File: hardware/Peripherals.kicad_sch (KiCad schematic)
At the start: 29 parts

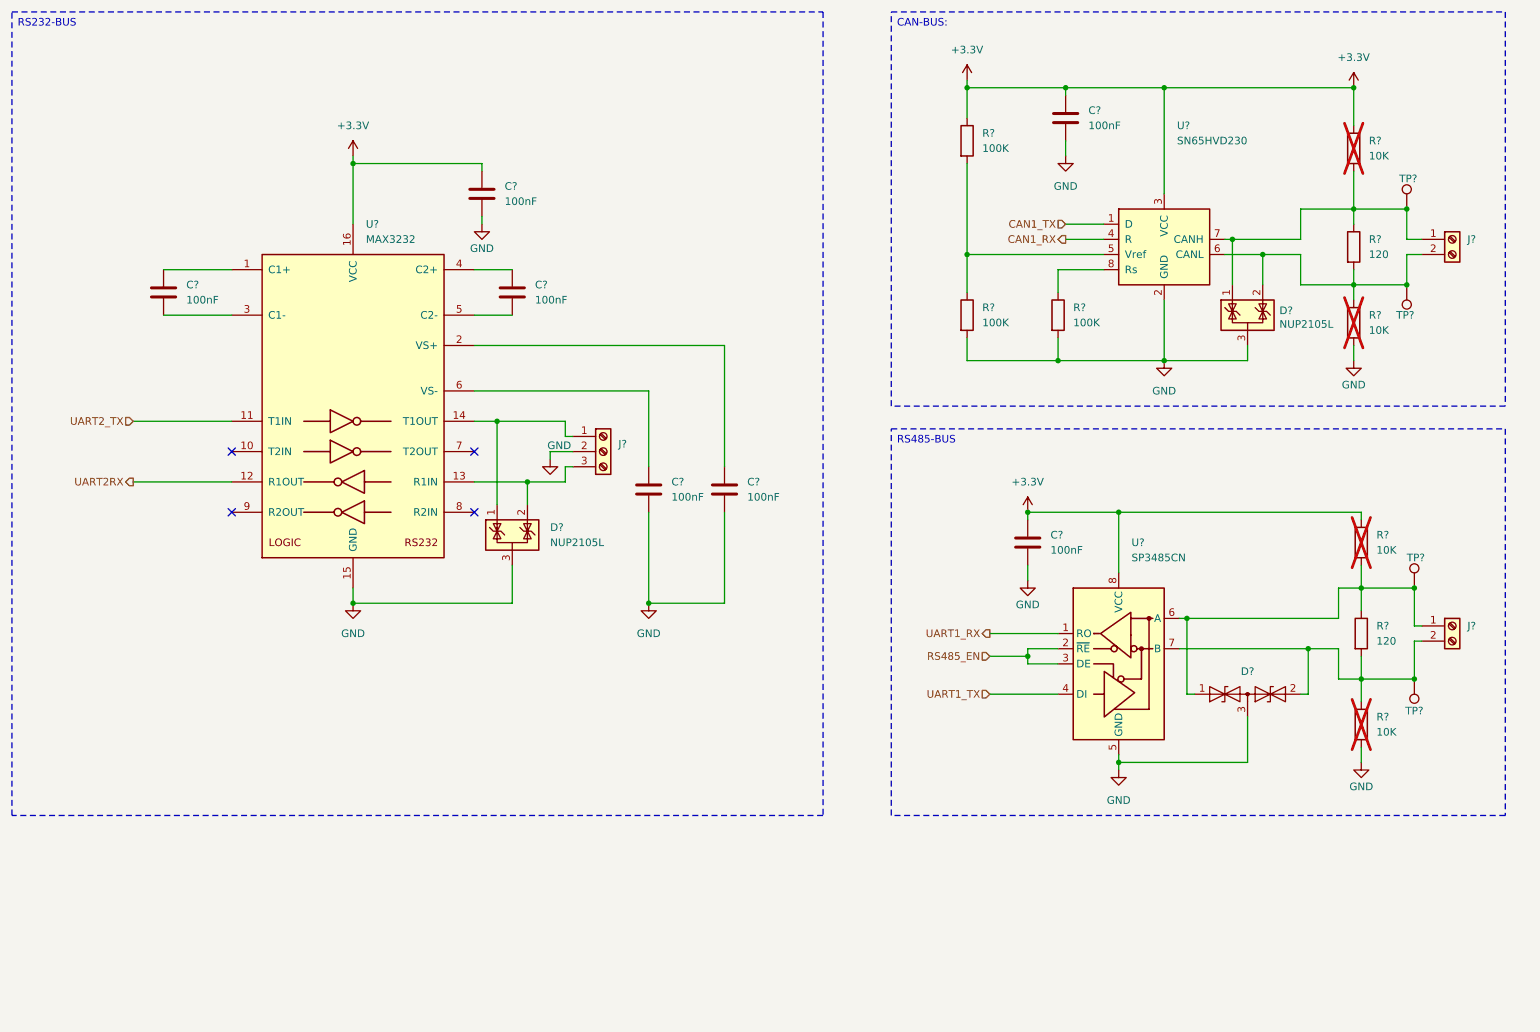
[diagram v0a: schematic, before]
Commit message: Change ESP32 module to stand-alone, change regulator for wide input range, modify location of certain things on MCU_Unit.
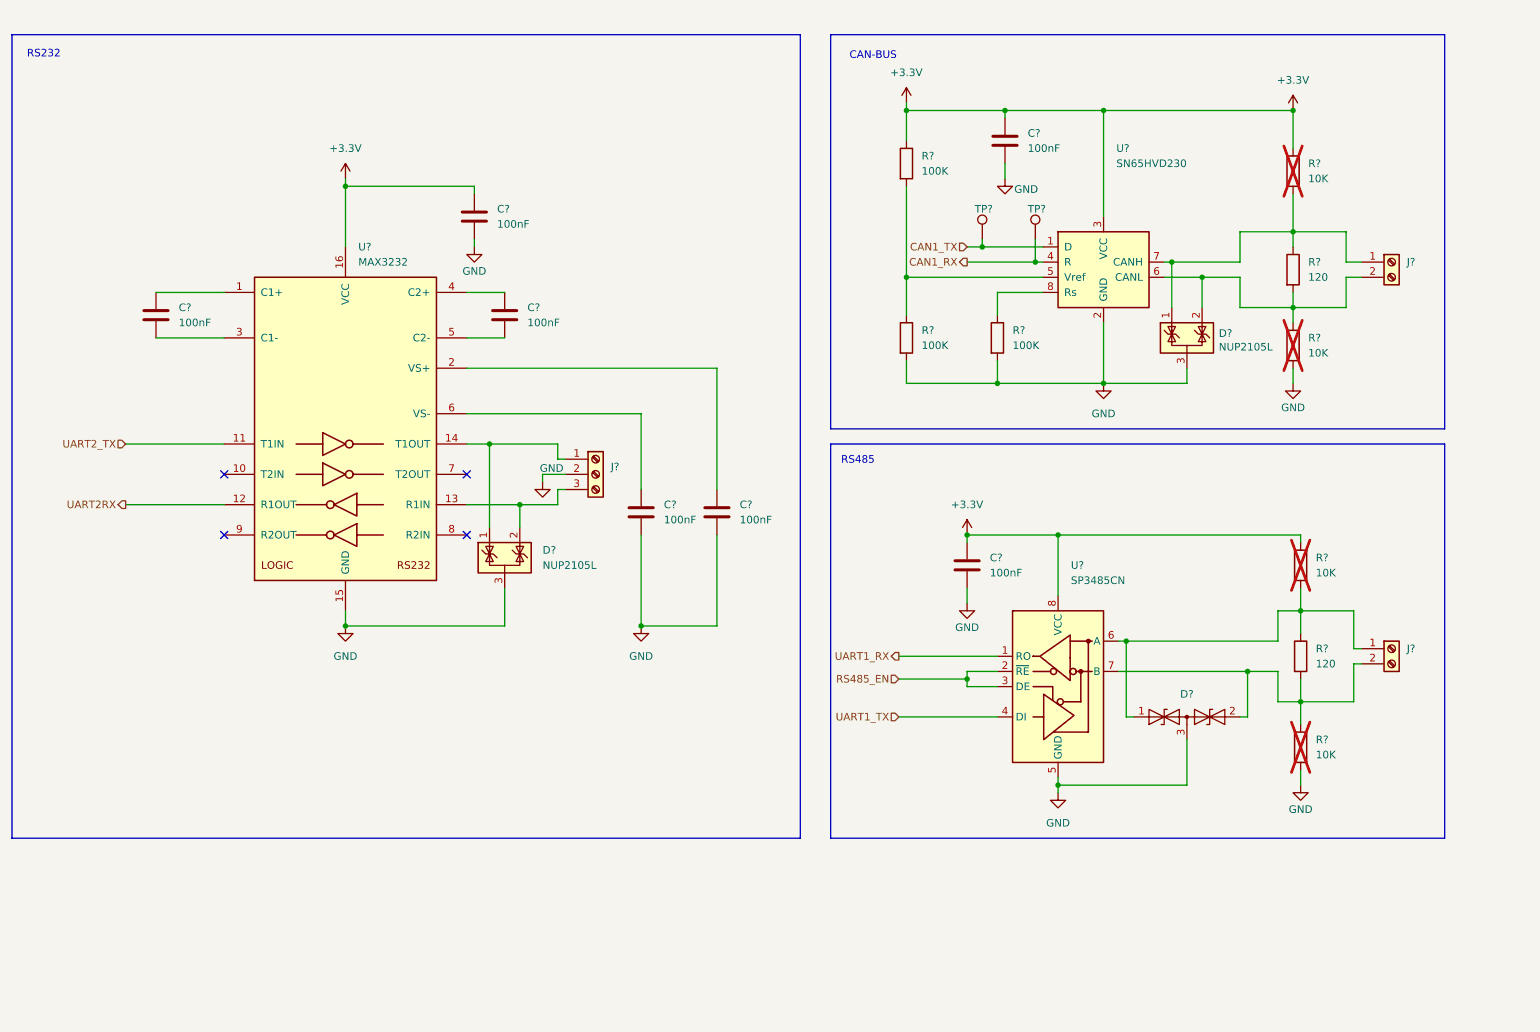
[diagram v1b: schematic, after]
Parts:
- removed TP? (x3): TestPoint, symbol Connector:TestPoint
- added TP?: TestPoint, symbol Connector:TestPoint
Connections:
- net CAN1_RX: now also TP?.1
- net CAN1_TX: now also TP?.1
- net at D?.2 (K), J?.2 (Pin_2), R?.1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: no longer TP?.1
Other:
- note added: "CAN-BUS"
- note added: "RS232"
- note added: "RS485"
- moved on the sheet: C?, D?, J?, R?, TP?, U?

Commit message: Assign footprints to some components and improvements.
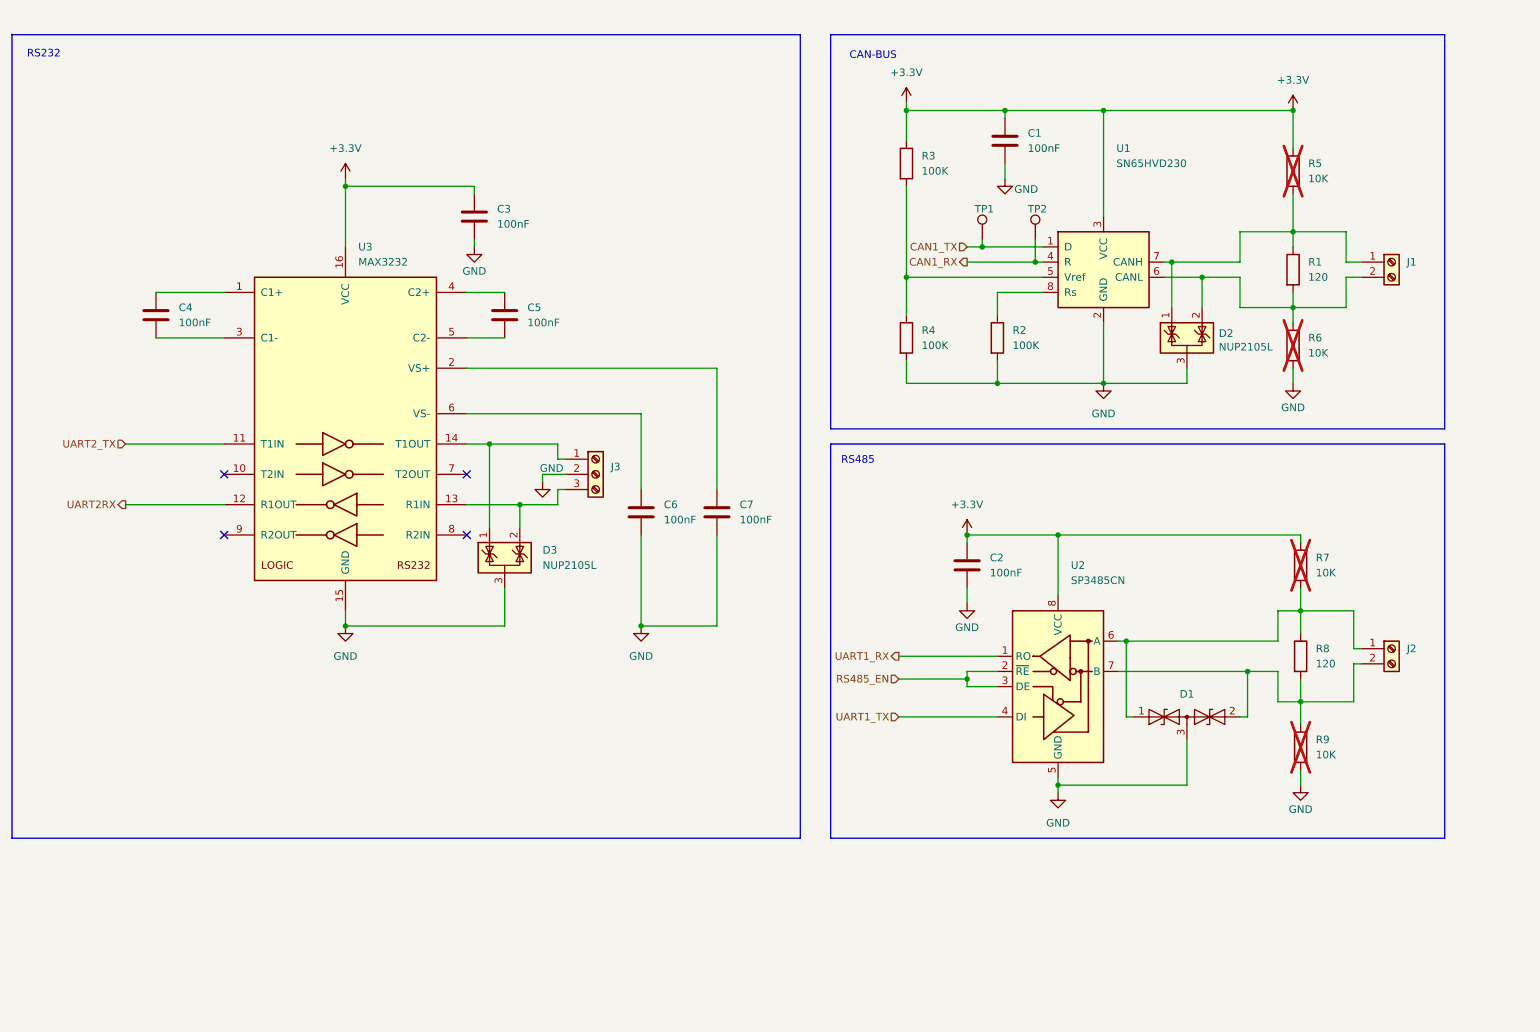
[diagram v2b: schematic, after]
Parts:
- R1, R2, R3, R4, R5, R6, R8: renamed from R?; footprint (none) -> Resistor_SMD:R_0805_2012Metric_Pad1.20x1.40mm_HandSolder
- U3: renamed from U?; footprint (none) -> Package_SO:TSSOP-16_4.4x5mm_P0.65mm
- gave numbers to parts that had none: 19
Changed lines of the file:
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@@
 		(dnp no)
 		(fields_autoplaced yes)
-		(property "Reference" "#PWR?"
+		(property "Reference" "#PWR013"
 			(at 130.81 130.81 0)
 			(effects
@@
 		(dnp no)
 		(fields_autoplaced yes)
-		(property "Reference" "#PWR?"
+		(property "Reference" "#PWR012"
 			(at 81.28 53.34 0)
 			(effects
@@
 		(dnp no)
 		(fields_autoplaced yes)
-		(property "Reference" "U?"
+		(property "Reference" "U3"
 			(at 83.4233 60.96 0)
 			(effects
@@
 			)
 		)
-		(property "Footprint" ""
+		(property "Footprint" "Package_SO:TSSOP-16_4.4x5mm_P0.65mm"
 			(at 82.55 118.11 0)
 			(effects
@@
 		(on_board yes)
 		(dnp no)
-		(property "Reference" "D?"
+		(property "Reference" "D2"
 			(at 227.584 75.438 0)
 			(effects
@@
 		(dnp no)
 		(fields_autoplaced yes)
-		(property "Reference" "C?"
+		(property "Reference" "C5"
 			(at 111.76 71.1199 0)
 			(effects
@@
 		(dnp no)
 		(fields_autoplaced yes)
-		(property "Reference" "#PWR?"
+		(property "Reference" "#PWR07"
 			(at 185.42 113.03 0)
 			(effects
@@
 		(on_board yes)
 		(dnp no)
-		(property "Reference" "U?"
+		(property "Reference" "U1"
 			(at 210.4233 44.45 0)
 			(effects
@@
 		(dnp no)
 		(fields_autoplaced yes)
-		(property "Reference" "R?"
+		(property "Reference" "R3"
 			(at 177.8 45.7199 0)
 			(effects
@@
 			)
 		)
-		(property "Footprint" ""
+		(property "Footprint" "Resistor_SMD:R_0805_2012Metric_Pad1.20x1.40mm_HandSolder"
 			(at 173.482 46.99 90)
 			(effects
@@
 		(dnp no)
 		(fields_autoplaced yes)
-		(property "Reference" "R?"
+		(property "Reference" "R2"
 			(at 193.04 74.9299 0)
 			(effects
@@
 			)
 		)
-		(property "Footprint" ""
+		(property "Footprint" "Resistor_SMD:R_0805_2012Metric_Pad1.20x1.40mm_HandSolder"
 			(at 188.722 76.2 90)
 			(effects
@@
 		(dnp yes)
 		(fields_autoplaced yes)
-		(property "Reference" "R?"
+		(property "Reference" "R5"
 			(at 242.57 46.9899 0)
 			(effects
@@
 			)
 		)
-		(property "Footprint" ""
+		(property "Footprint" "Resistor_SMD:R_0805_2012Metric_Pad1.20x1.40mm_HandSolder"
 			(at 238.252 48.26 90)
 			(effects
@@
 		(dnp no)
 		(fields_autoplaced yes)
-		(property "Reference" "J?"
+		(property "Reference" "J3"
 			(at 125.73 97.7899 0)
 			(effects
@@
 		(dnp no)
 		(fields_autoplaced yes)
-		(property "Reference" "#PWR?"
+		(property "Reference" "#PWR03"
 			(at 208.28 90.17 0)
 			(effects
@@
 		(dnp no)
 		(fields_autoplaced yes)
-		(property "Reference" "D?"
+		(property "Reference" "D1"
 			(at 222.25 135.89 0)
 			(effects
@@
 		(dnp yes)
 		(fields_autoplaced yes)
-		(property "Reference" "R?"
+		(property "Reference" "R9"
 			(at 243.84 143.5099 0)
 			(effects
@@
 		(dnp no)
 		(fields_autoplaced yes)
-		(property "Reference" "C?"
+		(property "Reference" "C7"
 			(at 147.32 104.1399 0)
 			(effects
@@
 		(on_board yes)
 		(dnp no)
-		(property "Reference" "#PWR?"
+		(property "Reference" "#PWR05"
 			(at 240.03 90.17 0)
 			(effects
@@
 		(dnp no)
 		(fields_autoplaced yes)
-		(property "Reference" "#PWR?"
+		(property "Reference" "#PWR01"
 			(at 175.26 40.64 0)
 			(effects
@@
 		(on_board yes)
 		(dnp no)
-		(property "Reference" "R?"
+		(property "Reference" "R8"
 			(at 243.84 128.2699 0)
 			(effects
@@
 			)
 		)
-		(property "Footprint" ""
+		(property "Footprint" "Resistor_SMD:R_0805_2012Metric_Pad1.20x1.40mm_HandSolder"
 			(at 239.522 129.54 90)
 			(effects
@@
 		(dnp no)
 		(fields_autoplaced yes)
-		(property "Reference" "C?"
+		(property "Reference" "C1"
 			(at 195.58 41.9099 0)
 			(effects
@@
 		(on_board yes)
 		(dnp no)
-		(property "Reference" "#PWR?"
+		(property "Reference" "#PWR09"
 			(at 191.77 55.88 0)
 			(effects
@@
 		(dnp no)
 		(fields_autoplaced yes)
-		(property "Reference" "C?"
+		(property "Reference" "C6"
 			(at 134.62 104.1399 0)
 			(effects
@@
 		(dnp no)
 		(fields_autoplaced yes)
-		(property "Reference" "C?"
+		(property "Reference" "C2"
 			(at 189.23 113.0299 0)
 			(effects
@@
 		(dnp no)
 		(fields_autoplaced yes)
-		(property "Reference" "C?"
+		(property "Reference" "C4"
 			(at 53.34 71.1199 0)
 			(effects
@@
 		(on_board yes)
 		(dnp no)
-		(property "Reference" "#PWR?"
+		(property "Reference" "#PWR08"
 			(at 185.42 127 0)
 			(effects
@@
 		(on_board yes)
 		(dnp no)
-		(property "Reference" "R?"
+		(property "Reference" "R1"
 			(at 242.57 63.4999 0)
 			(effects
@@
 			)
 		)
-		(property "Footprint" ""
+		(property "Footprint" "Resistor_SMD:R_0805_2012Metric_Pad1.20x1.40mm_HandSolder"
 			(at 238.252 64.77 90)
 			(effects
@@
 		(on_board yes)
 		(dnp no)
-		(property "Reference" "TP?"
+		(property "Reference" "TP1"
 			(at 186.69 54.61 0)
 			(effects
@@
 		(on_board yes)
 		(dnp no)
-		(property "Reference" "#PWR?"
+		(property "Reference" "#PWR06"
 			(at 241.3 157.48 0)
 			(effects
@@
 		(on_board yes)
 		(dnp no)
-		(property "Reference" "TP?"
+		(property "Reference" "TP2"
 			(at 195.58 54.61 0)
 			(effects
@@
 		(dnp no)
 		(fields_autoplaced yes)
-		(property "Reference" "R?"
+		(property "Reference" "R4"
 			(at 177.8 74.9299 0)
 			(effects
@@
 			)
 		)
-		(property "Footprint" ""
+		(property "Footprint" "Resistor_SMD:R_0805_2012Metric_Pad1.20x1.40mm_HandSolder"
 			(at 173.482 76.2 90)
 			(effects
@@
 		(dnp no)
 		(fields_autoplaced yes)
-		(property "Reference" "#PWR?"
+		(property "Reference" "#PWR04"
 			(at 200.66 158.75 0)
 			(effects
@@
 		(dnp no)
 		(fields_autoplaced yes)
-		(property "Reference" "J?"
+		(property "Reference" "J2"
 			(at 259.08 128.2699 0)
 			(effects
@@
 		(dnp yes)
 		(fields_autoplaced yes)
-		(property "Reference" "R?"
+		(property "Reference" "R7"
 			(at 243.84 113.0299 0)
 			(effects
@@
 		(dnp no)
 		(fields_autoplaced yes)
-		(property "Reference" "J?"
+		(property "Reference" "J1"
 			(at 259.08 63.4999 0)
 			(effects
@@
 		(on_board yes)
 		(dnp no)
-		(property "Reference" "#PWR?"
+		(property "Reference" "#PWR014"
 			(at 114.3 106.68 0)
 			(effects
@@
 		(on_board yes)
 		(dnp no)
-		(property "Reference" "#PWR?"
+		(property "Reference" "#PWR011"
 			(at 102.87 67.31 0)
 			(effects
@@
 		(dnp no)
 		(fields_autoplaced yes)
-		(property "Reference" "#PWR?"
+		(property "Reference" "#PWR02"
 			(at 240.03 41.91 0)
 			(effects
@@
 		(dnp no)
 		(fields_autoplaced yes)
-		(property "Reference" "C?"
+		(property "Reference" "C3"
 			(at 106.68 54.6099 0)
 			(effects
@@
 		(dnp no)
 		(fields_autoplaced yes)
-		(property "Reference" "D?"
+		(property "Reference" "D3"
 			(at 114.3 111.7599 0)
 			(effects
@@
 		(dnp no)
 		(fields_autoplaced yes)
-		(property "Reference" "#PWR?"
+		(property "Reference" "#PWR010"
 			(at 81.28 130.81 0)
 			(effects
@@
 		(dnp yes)
 		(fields_autoplaced yes)
-		(property "Reference" "R?"
+		(property "Reference" "R6"
 			(at 242.57 76.1999 0)
 			(effects
@@
 			)
 		)
-		(property "Footprint" ""
+		(property "Footprint" "Resistor_SMD:R_0805_2012Metric_Pad1.20x1.40mm_HandSolder"
 			(at 238.252 77.47 90)
 			(effects
@@
 		(on_board yes)
 		(dnp no)
-		(property "Reference" "U?"
+		(property "Reference" "U2"
 			(at 202.8033 114.3 0)
 			(effects

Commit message: Improvements to schematic.
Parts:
- renumbered C5 to C?, C7 to C?, C1 to C?, C6 to C?, C2 to C?, C4 to C?, C3 to C?, D2 to D?, D1 to D?, D3 to D?, J3 to J?, J2 to J?, J1 to J?, R3 to R?, R2 to R?, R5 to R?, R9 to R?, R8 to R?, R1 to R?, R4 to R?, R7 to R?, R6 to R?, TP1 to TP?, TP2 to TP?, U3 to U?, U1 to U?, U2 to U?
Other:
- company: (none) -> FEYTECH PTY LTD
- title: (none) -> MQTT Gateway
- moved on the sheet: J?

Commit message: Add footprint to components
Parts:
- C? (x7): footprint Capacitor_SMD:C_0805_2012Metric_Pad1.18x1.45mm_HandSolder -> Capacitor_SMD:C_0603_1608Metric_Pad1.08x0.95mm_HandSolder
- R? (x7): footprint Resistor_SMD:R_0805_2012Metric_Pad1.20x1.40mm_HandSolder -> Resistor_SMD:R_0603_1608Metric_Pad0.98x0.95mm_HandSolder
- R? (x2): footprint (none) -> Resistor_SMD:R_0603_1608Metric_Pad0.98x0.95mm_HandSolder
- TP? (x2): footprint (none) -> TestPoint:TestPoint_Pad_D1.0mm
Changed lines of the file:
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@@
 			)
 		)
-		(property "Footprint" "Capacitor_SMD:C_0805_2012Metric_Pad1.18x1.45mm_HandSolder"
+		(property "Footprint" "Capacitor_SMD:C_0603_1608Metric_Pad1.08x0.95mm_HandSolder"
 			(at 108.9152 76.2 0)
 			(effects
@@
 			)
 		)
-		(property "Footprint" "Resistor_SMD:R_0805_2012Metric_Pad1.20x1.40mm_HandSolder"
+		(property "Footprint" "Resistor_SMD:R_0603_1608Metric_Pad0.98x0.95mm_HandSolder"
 			(at 173.482 46.99 90)
 			(effects
@@
 			)
 		)
-		(property "Footprint" "Resistor_SMD:R_0805_2012Metric_Pad1.20x1.40mm_HandSolder"
+		(property "Footprint" "Resistor_SMD:R_0603_1608Metric_Pad0.98x0.95mm_HandSolder"
 			(at 188.722 76.2 90)
 			(effects
@@
 			)
 		)
-		(property "Footprint" "Resistor_SMD:R_0805_2012Metric_Pad1.20x1.40mm_HandSolder"
+		(property "Footprint" "Resistor_SMD:R_0603_1608Metric_Pad0.98x0.95mm_HandSolder"
 			(at 238.252 48.26 90)
 			(effects
@@
 			)
 		)
-		(property "Footprint" ""
+		(property "Footprint" "Resistor_SMD:R_0603_1608Metric_Pad0.98x0.95mm_HandSolder"
 			(at 239.522 144.78 90)
 			(effects
@@
 			)
 		)
-		(property "Footprint" "Capacitor_SMD:C_0805_2012Metric_Pad1.18x1.45mm_HandSolder"
+		(property "Footprint" "Capacitor_SMD:C_0603_1608Metric_Pad1.08x0.95mm_HandSolder"
 			(at 144.4752 109.22 0)
 			(effects
@@
 			)
 		)
-		(property "Footprint" "Resistor_SMD:R_0805_2012Metric_Pad1.20x1.40mm_HandSolder"
+		(property "Footprint" "Resistor_SMD:R_0603_1608Metric_Pad0.98x0.95mm_HandSolder"
 			(at 239.522 129.54 90)
 			(effects
@@
 			)
 		)
-		(property "Footprint" "Capacitor_SMD:C_0805_2012Metric_Pad1.18x1.45mm_HandSolder"
+		(property "Footprint" "Capacitor_SMD:C_0603_1608Metric_Pad1.08x0.95mm_HandSolder"
 			(at 192.7352 46.99 0)
 			(effects
@@
 			)
 		)
-		(property "Footprint" "Capacitor_SMD:C_0805_2012Metric_Pad1.18x1.45mm_HandSolder"
+		(property "Footprint" "Capacitor_SMD:C_0603_1608Metric_Pad1.08x0.95mm_HandSolder"
 			(at 131.7752 109.22 0)
 			(effects
@@
 			)
 		)
-		(property "Footprint" "Capacitor_SMD:C_0805_2012Metric_Pad1.18x1.45mm_HandSolder"
+		(property "Footprint" "Capacitor_SMD:C_0603_1608Metric_Pad1.08x0.95mm_HandSolder"
 			(at 186.3852 118.11 0)
 			(effects
@@
 			)
 		)
-		(property "Footprint" "Capacitor_SMD:C_0805_2012Metric_Pad1.18x1.45mm_HandSolder"
+		(property "Footprint" "Capacitor_SMD:C_0603_1608Metric_Pad1.08x0.95mm_HandSolder"
 			(at 50.4952 76.2 0)
 			(effects
@@
 			)
 		)
-		(property "Footprint" "Resistor_SMD:R_0805_2012Metric_Pad1.20x1.40mm_HandSolder"
+		(property "Footprint" "Resistor_SMD:R_0603_1608Metric_Pad0.98x0.95mm_HandSolder"
 			(at 238.252 64.77 90)
 			(effects
@@
 			)
 		)
-		(property "Footprint" ""
+		(property "Footprint" "TestPoint:TestPoint_Pad_D1.0mm"
 			(at 193.04 59.69 0)
 			(effects
@@
 			)
 		)
-		(property "Footprint" ""
+		(property "Footprint" "TestPoint:TestPoint_Pad_D1.0mm"
 			(at 201.93 59.69 0)
 			(effects
@@
 			)
 		)
-		(property "Footprint" "Resistor_SMD:R_0805_2012Metric_Pad1.20x1.40mm_HandSolder"
+		(property "Footprint" "Resistor_SMD:R_0603_1608Metric_Pad0.98x0.95mm_HandSolder"
 			(at 173.482 76.2 90)
 			(effects
@@
 			)
 		)
-		(property "Footprint" ""
+		(property "Footprint" "Resistor_SMD:R_0603_1608Metric_Pad0.98x0.95mm_HandSolder"
 			(at 239.522 114.3 90)
 			(effects
@@
 			)
 		)
-		(property "Footprint" "Capacitor_SMD:C_0805_2012Metric_Pad1.18x1.45mm_HandSolder"
+		(property "Footprint" "Capacitor_SMD:C_0603_1608Metric_Pad1.08x0.95mm_HandSolder"
 			(at 103.8352 59.69 0)
 			(effects
@@
 			)
 		)
-		(property "Footprint" "Resistor_SMD:R_0805_2012Metric_Pad1.20x1.40mm_HandSolder"
+		(property "Footprint" "Resistor_SMD:R_0603_1608Metric_Pad0.98x0.95mm_HandSolder"
 			(at 238.252 77.47 90)
 			(effects

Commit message: Improvements
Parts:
- J3: renamed from J?; footprint (none) -> TerminalBlock_Phoenix:TerminalBlock_Phoenix_MKDS-1,5-3-5.08_1x03_P5.08mm_Horizontal
- J4, J5: renamed from J?; footprint (none) -> TerminalBlock_Phoenix:TerminalBlock_Phoenix_MKDS-1,5-2-5.08_1x02_P5.08mm_Horizontal
- gave numbers to parts that had none: 24
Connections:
- net UART2RX renamed UART2_RX
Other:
- moved on the sheet: J5
